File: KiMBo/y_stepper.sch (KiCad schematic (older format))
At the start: 25 parts, among them U24 TMC2130

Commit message: Assocate more footprints
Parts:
- C181, C182: footprint Capacitors_SMD:C_0402 -> Capacitors_SMD:C_0603
- R173, R174, R175, R176, R177, R178: footprint (none) -> Resistors_SMD:R_0603
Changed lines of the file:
@@
 F 0 "C182" H 8315 4346 50  0000 L CNN
 F 1 "22nF" H 8315 4255 50  0000 L CNN
-F 2 "Capacitors_SMD:C_0402" H 8238 4150 50  0001 C CNN
+F 2 "Capacitors_SMD:C_0603" H 8238 4150 50  0001 C CNN
 F 3 "" H 8200 4300 50  0000 C CNN
 	1    8200 4300
@@
 F 0 "R176" V 6250 3900 50  0000 C CNN
 F 1 "2.2Ω" V 6350 3900 50  0000 C CNN
-F 2 "" V 6280 3900 50  0001 C CNN
+F 2 "Resistors_SMD:R_0603" V 6280 3900 50  0001 C CNN
 F 3 "" H 6350 3900 50  0000 C CNN
 	1    6350 3900
@@
 F 0 "R174" H 5169 4446 50  0000 L CNN
 F 1 "4.7kΩ" H 5169 4355 50  0000 L CNN
-F 2 "" V 5030 4400 50  0001 C CNN
+F 2 "Resistors_SMD:R_0603" V 5030 4400 50  0001 C CNN
 F 3 "" H 5100 4400 50  0000 C CNN
 	1    5100 4400
@@
 F 0 "C181" H 6600 4200 50  0000 L CNN
 F 1 "4.7μF" H 6600 4000 50  0000 L CNN
-F 2 "Capacitors_SMD:C_0402" H 6588 3950 50  0001 C CNN
+F 2 "Capacitors_SMD:C_0603" H 6588 3950 50  0001 C CNN
 F 3 "" H 6550 4100 50  0000 C CNN
 	1    6550 4100
@@
 F 0 "R177" H 8369 6896 50  0000 L CNN
 F 1 "5.23kΩ" H 8369 6805 50  0000 L CNN
-F 2 "" V 8230 6850 50  0001 C CNN
+F 2 "Resistors_SMD:R_0603" V 8230 6850 50  0001 C CNN
 F 3 "" H 8300 6850 50  0000 C CNN
 	1    8300 6850
@@
 F 0 "R178" V 8300 7050 50  0000 C CNN
 F 1 "4.75kΩ" V 8400 7050 50  0000 C CNN
-F 2 "" V 8430 7050 50  0001 C CNN
+F 2 "Resistors_SMD:R_0603" V 8430 7050 50  0001 C CNN
 F 3 "" H 8500 7050 50  0000 C CNN
 	1    8500 7050
@@
 F 0 "R175" H 5519 4446 50  0000 L CNN
 F 1 "4.7kΩ" H 5519 4355 50  0000 L CNN
-F 2 "" V 5380 4400 50  0001 C CNN
+F 2 "Resistors_SMD:R_0603" V 5380 4400 50  0001 C CNN
 F 3 "" H 5450 4400 50  0000 C CNN
 	1    5450 4400
@@
 F 0 "R173" H 4819 4446 50  0000 L CNN
 F 1 "4.7kΩ" H 4819 4355 50  0000 L CNN
-F 2 "" V 4680 4400 50  0001 C CNN
+F 2 "Resistors_SMD:R_0603" V 4680 4400 50  0001 C CNN
 F 3 "" H 4750 4400 50  0000 C CNN
 	1    4750 4400

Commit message: More footprint association
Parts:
- R179, R180: footprint (none) -> Resistors_SMD:R_0805
- U24: footprint (none) -> KiMBo:QFN36_5X6
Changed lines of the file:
@@
 $EndComp
 $Comp
-L GND #PWR0242
+L GND #PWR0243
 U 1 1 58C0B231
 P 6550 3450
-F 0 "#PWR0242" H 6550 3200 50  0001 C CNN
+F 0 "#PWR0243" H 6550 3200 50  0001 C CNN
 F 1 "GND" H 6550 3300 50  0000 C CNN
 F 2 "" H 6550 3450 50  0000 C CNN
@@
 $EndComp
 $Comp
-L GND #PWR0243
+L GND #PWR0244
 U 1 1 58C0B23E
 P 9400 3500
-F 0 "#PWR0243" H 9400 3250 50  0001 C CNN
+F 0 "#PWR0244" H 9400 3250 50  0001 C CNN
 F 1 "GND" H 9405 3327 50  0000 C CNN
 F 2 "" H 9400 3500 50  0000 C CNN
@@
 $EndComp
 $Comp
-L +24V #PWR0244
+L +24V #PWR0245
 U 1 1 58C0B244
 P 7600 3000
-F 0 "#PWR0244" H 7600 2850 50  0001 C CNN
+F 0 "#PWR0245" H 7600 2850 50  0001 C CNN
 F 1 "+24V" H 7615 3173 50  0000 C CNN
 F 2 "" H 7600 3000 50  0000 C CNN
@@
 F 0 "R180" H 9750 6800 50  0000 R CNN
 F 1 "220mΩ" H 9750 6900 50  0000 R CNN
-F 2 "" V 9730 6850 50  0001 C CNN
+F 2 "Resistors_SMD:R_0805" V 9730 6850 50  0001 C CNN
 F 3 "" H 9800 6850 50  0000 C CNN
 	1    9800 6850
@@
 F 0 "R179" H 8950 6800 50  0000 R CNN
 F 1 "220mΩ" H 8950 6900 50  0000 R CNN
-F 2 "" V 8930 6850 50  0001 C CNN
+F 2 "Resistors_SMD:R_0805" V 8930 6850 50  0001 C CNN
 F 3 "" H 9000 6850 50  0000 C CNN
 	1    9000 6850
@@
 $EndComp
 $Comp
-L GND #PWR0245
+L GND #PWR0246
 U 1 1 58C0B25F
 P 8700 7200
-F 0 "#PWR0245" H 8700 6950 50  0001 C CNN
+F 0 "#PWR0246" H 8700 6950 50  0001 C CNN
 F 1 "GND" H 8705 7027 50  0000 C CNN
 F 2 "" H 8700 7200 50  0000 C CNN
@@
 NoConn ~ 6750 5850
 $Comp
-L GND #PWR0246
+L GND #PWR0247
 U 1 1 58C0B282
 P 6700 6250
-F 0 "#PWR0246" H 6700 6000 50  0001 C CNN
+F 0 "#PWR0247" H 6700 6000 50  0001 C CNN
 F 1 "GND" H 6705 6077 50  0000 C CNN
 F 2 "" H 6700 6250 50  0000 C CNN
@@
 $EndComp
 $Comp
-L GND #PWR0247
+L GND #PWR0248
 U 1 1 58C0B2C6
 P 8300 5350
-F 0 "#PWR0247" H 8300 5100 50  0001 C CNN
+F 0 "#PWR0248" H 8300 5100 50  0001 C CNN
 F 1 "GND" H 8300 5200 50  0000 C CNN
 F 2 "" H 8300 5350 50  0000 C CNN
@@
 $EndComp
 $Comp
-L GND #PWR0248
+L GND #PWR0249
 U 1 1 58C0B2DA
 P 8300 6200
-F 0 "#PWR0248" H 8300 5950 50  0001 C CNN
+F 0 "#PWR0249" H 8300 5950 50  0001 C CNN
 F 1 "GND" H 8300 6050 50  0000 C CNN
 F 2 "" H 8300 6200 50  0000 C CNN
@@
 F 0 "U24" H 7000 6350 60  0000 C CNN
 F 1 "TMC2130" H 7750 6350 60  0000 C CNN
-F 2 "" H 7450 5150 60  0001 C CNN
+F 2 "KiMBo:QFN36_5X6" H 7450 5150 60  0001 C CNN
 F 3 "" H 7450 5150 60  0000 C CNN
 	1    7450 4850
@@
 	4750 3650 6750 3650
 $Comp
-L VDD_3V3B #PWR0249
+L VDD_3V3B #PWR0250
 U 1 1 5A300CA5
 P 5800 3600
-F 0 "#PWR0249" H 5800 3450 50  0001 C CNN
+F 0 "#PWR0250" H 5800 3450 50  0001 C CNN
 F 1 "VDD_3V3B" H 5815 3773 50  0000 C CNN
 F 2 "" H 5800 3600 50  0000 C CNN

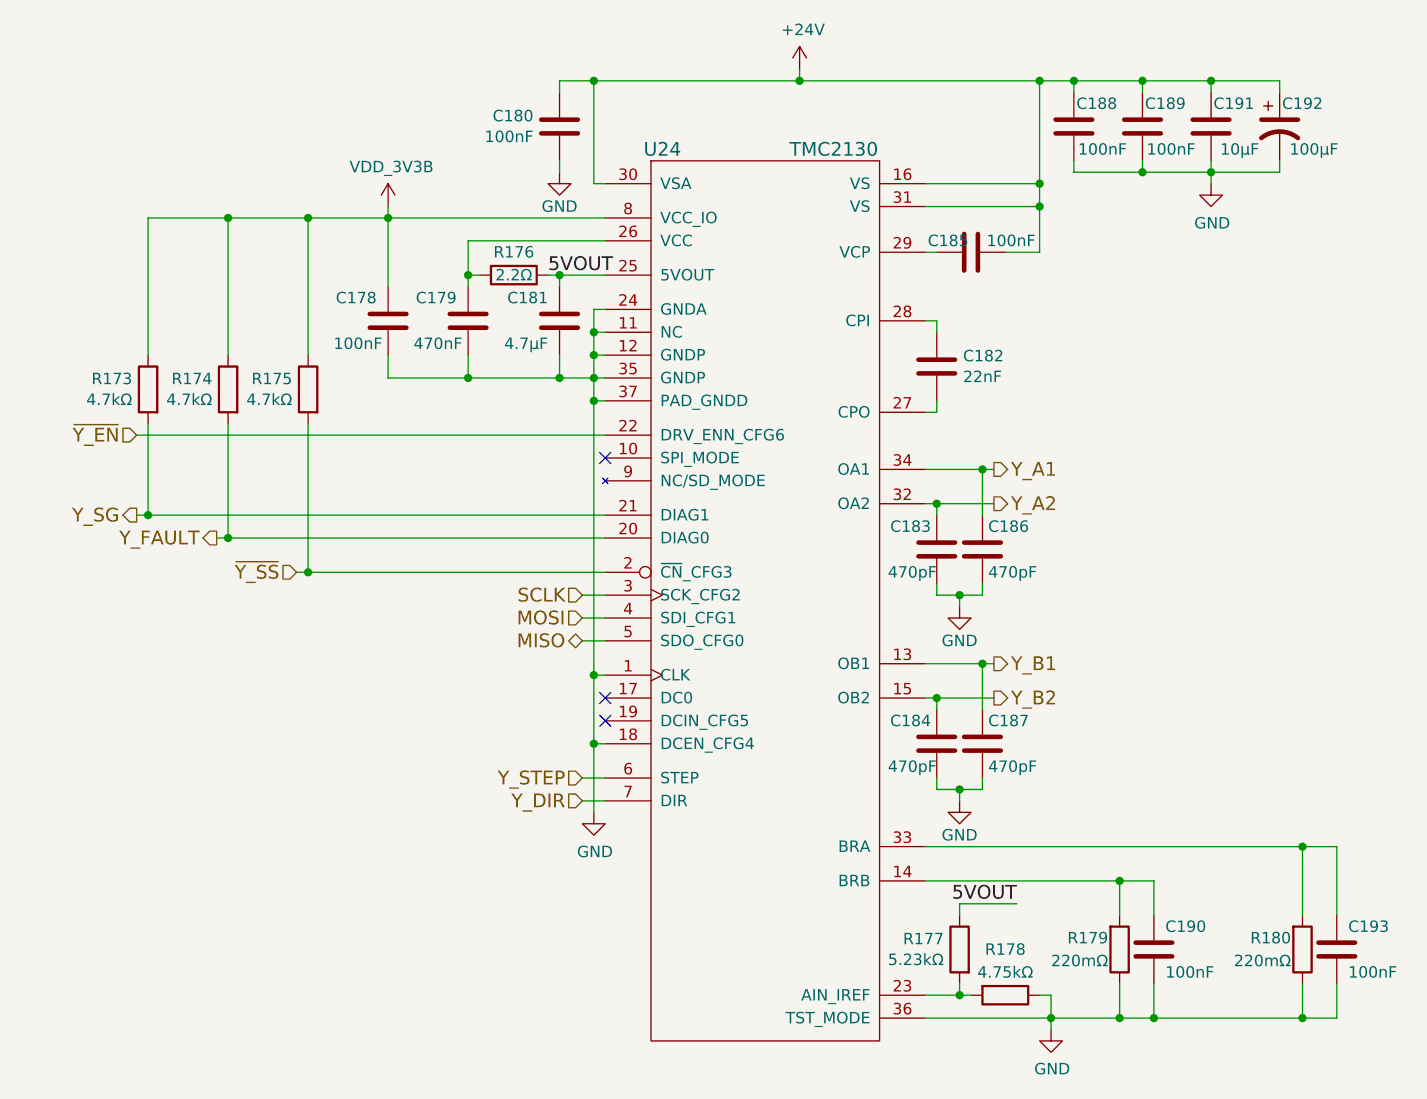
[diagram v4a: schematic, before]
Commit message: Add more footprints and more associations, one association left!
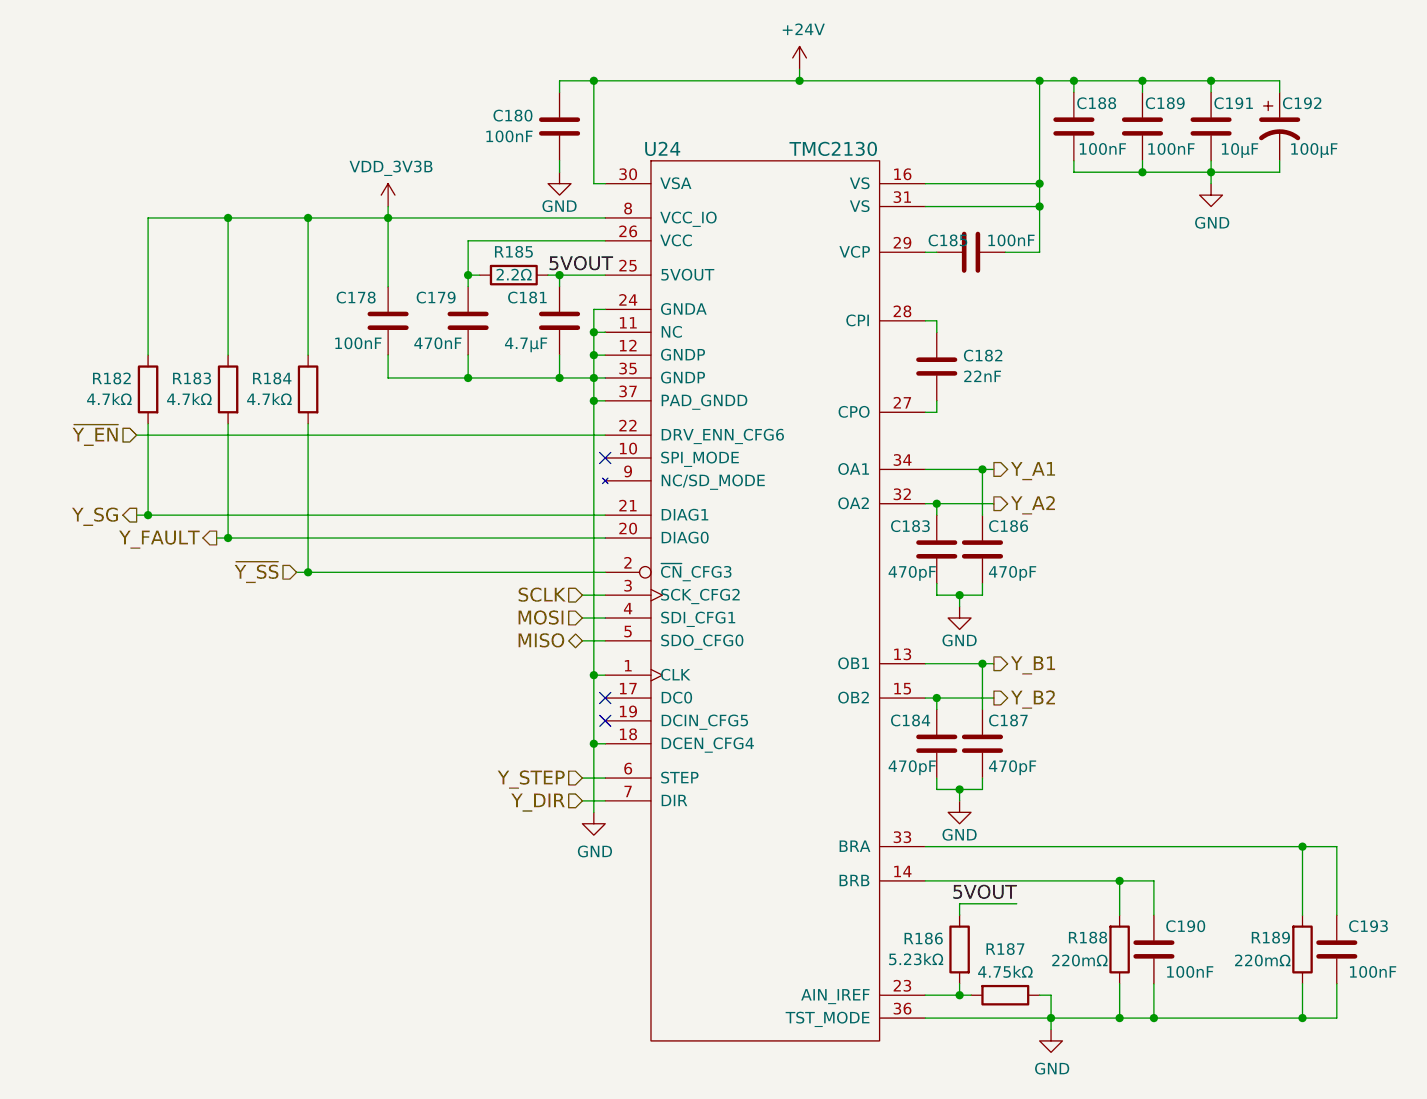
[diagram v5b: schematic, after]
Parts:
- R187: renamed from R178; footprint Resistors_SMD:R_0603 -> Resistors_SMD:R_0805
- R189: renamed from R180; footprint Resistors_SMD:R_0805 -> Resistors_SMD:R_0603
- renumbered R173 to R182, R174 to R183, R175 to R184, R176 to R185, R177 to R186, R179 to R188
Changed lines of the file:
@@
 $EndComp
 $Comp
-L GND #PWR0243
+L GND #PWR0245
 U 1 1 58C0B231
 P 6550 3450
-F 0 "#PWR0243" H 6550 3200 50  0001 C CNN
+F 0 "#PWR0245" H 6550 3200 50  0001 C CNN
 F 1 "GND" H 6550 3300 50  0000 C CNN
 F 2 "" H 6550 3450 50  0000 C CNN
@@
 $EndComp
 $Comp
-L GND #PWR0244
+L GND #PWR0246
 U 1 1 58C0B23E
 P 9400 3500
-F 0 "#PWR0244" H 9400 3250 50  0001 C CNN
+F 0 "#PWR0246" H 9400 3250 50  0001 C CNN
 F 1 "GND" H 9405 3327 50  0000 C CNN
 F 2 "" H 9400 3500 50  0000 C CNN
@@
 $EndComp
 $Comp
-L +24V #PWR0245
+L +24V #PWR0247
 U 1 1 58C0B244
 P 7600 3000
-F 0 "#PWR0245" H 7600 2850 50  0001 C CNN
+F 0 "#PWR0247" H 7600 2850 50  0001 C CNN
 F 1 "+24V" H 7615 3173 50  0000 C CNN
 F 2 "" H 7600 3000 50  0000 C CNN
@@
 $EndComp
 $Comp
-L R R180
+L R R189
 U 1 1 58C0B251
 P 9800 6850
-F 0 "R180" H 9750 6800 50  0000 R CNN
+F 0 "R189" H 9750 6800 50  0000 R CNN
 F 1 "220mΩ" H 9750 6900 50  0000 R CNN
-F 2 "Resistors_SMD:R_0805" V 9730 6850 50  0001 C CNN
+F 2 "Resistors_SMD:R_0603" V 9730 6850 50  0001 C CNN
 F 3 "" H 9800 6850 50  0000 C CNN
 	1    9800 6850
@@
 $EndComp
 $Comp
-L R R179
+L R R188
 U 1 1 58C0B258
 P 9000 6850
-F 0 "R179" H 8950 6800 50  0000 R CNN
+F 0 "R188" H 8950 6800 50  0000 R CNN
 F 1 "220mΩ" H 8950 6900 50  0000 R CNN
 F 2 "Resistors_SMD:R_0805" V 8930 6850 50  0001 C CNN
@@
 $EndComp
 $Comp
-L GND #PWR0246
+L GND #PWR0248
 U 1 1 58C0B25F
 P 8700 7200
-F 0 "#PWR0246" H 8700 6950 50  0001 C CNN
+F 0 "#PWR0248" H 8700 6950 50  0001 C CNN
 F 1 "GND" H 8705 7027 50  0000 C CNN
 F 2 "" H 8700 7200 50  0000 C CNN
@@
 NoConn ~ 6750 5750
 $Comp
-L R R176
+L R R185
 U 1 1 58C0B266
 P 6350 3900
-F 0 "R176" V 6250 3900 50  0000 C CNN
+F 0 "R185" V 6250 3900 50  0000 C CNN
 F 1 "2.2Ω" V 6350 3900 50  0000 C CNN
 F 2 "Resistors_SMD:R_0603" V 6280 3900 50  0001 C CNN
@@
 NoConn ~ 6750 5850
 $Comp
-L GND #PWR0247
+L GND #PWR0249
 U 1 1 58C0B282
 P 6700 6250
-F 0 "#PWR0247" H 6700 6000 50  0001 C CNN
+F 0 "#PWR0249" H 6700 6000 50  0001 C CNN
 F 1 "GND" H 6705 6077 50  0000 C CNN
 F 2 "" H 6700 6250 50  0000 C CNN
@@
 Y_FAULT
 $Comp
-L R R174
+L R R183
 U 1 1 58C0B290
 P 5100 4400
-F 0 "R174" H 5169 4446 50  0000 L CNN
+F 0 "R183" H 5169 4446 50  0000 L CNN
 F 1 "4.7kΩ" H 5169 4355 50  0000 L CNN
 F 2 "Resistors_SMD:R_0603" V 5030 4400 50  0001 C CNN
@@
 5VOUT
 $Comp
-L R R177
+L R R186
 U 1 1 58C0B2A2
 P 8300 6850
-F 0 "R177" H 8369 6896 50  0000 L CNN
+F 0 "R186" H 8369 6896 50  0000 L CNN
 F 1 "5.23kΩ" H 8369 6805 50  0000 L CNN
 F 2 "Resistors_SMD:R_0603" V 8230 6850 50  0001 C CNN
@@
 5VOUT
 $Comp
-L R R178
+L R R187
 U 1 1 58C0B2AA
 P 8500 7050
-F 0 "R178" V 8300 7050 50  0000 C CNN
+F 0 "R187" V 8300 7050 50  0000 C CNN
 F 1 "4.75kΩ" V 8400 7050 50  0000 C CNN
-F 2 "Resistors_SMD:R_0603" V 8430 7050 50  0001 C CNN
+F 2 "Resistors_SMD:R_0805" V 8430 7050 50  0001 C CNN
 F 3 "" H 8500 7050 50  0000 C CNN
 	1    8500 7050
@@
 $EndComp
 $Comp
-L R R175
+L R R184
 U 1 1 58C0B2B1
 P 5450 4400
-F 0 "R175" H 5519 4446 50  0000 L CNN
+F 0 "R184" H 5519 4446 50  0000 L CNN
 F 1 "4.7kΩ" H 5519 4355 50  0000 L CNN
 F 2 "Resistors_SMD:R_0603" V 5380 4400 50  0001 C CNN
@@
 $EndComp
 $Comp
-L GND #PWR0248
+L GND #PWR0250
 U 1 1 58C0B2C6
 P 8300 5350
-F 0 "#PWR0248" H 8300 5100 50  0001 C CNN
+F 0 "#PWR0250" H 8300 5100 50  0001 C CNN
 F 1 "GND" H 8300 5200 50  0000 C CNN
 F 2 "" H 8300 5350 50  0000 C CNN
@@
 $EndComp
 $Comp
-L GND #PWR0249
+L GND #PWR0251
 U 1 1 58C0B2DA
 P 8300 6200
-F 0 "#PWR0249" H 8300 5950 50  0001 C CNN
+F 0 "#PWR0251" H 8300 5950 50  0001 C CNN
 F 1 "GND" H 8300 6050 50  0000 C CNN
 F 2 "" H 8300 6200 50  0000 C CNN
@@
 	8200 6150 8200 6100
 $Comp
-L R R173
+L R R182
 U 1 1 58C0B35B
 P 4750 4400
-F 0 "R173" H 4819 4446 50  0000 L CNN
+F 0 "R182" H 4819 4446 50  0000 L CNN
 F 1 "4.7kΩ" H 4819 4355 50  0000 L CNN
 F 2 "Resistors_SMD:R_0603" V 4680 4400 50  0001 C CNN
@@
 	4750 3650 6750 3650
 $Comp
-L VDD_3V3B #PWR0250
+L VDD_3V3B #PWR0252
 U 1 1 5A300CA5
 P 5800 3600
-F 0 "#PWR0250" H 5800 3450 50  0001 C CNN
+F 0 "#PWR0252" H 5800 3450 50  0001 C CNN
 F 1 "VDD_3V3B" H 5815 3773 50  0000 C CNN
 F 2 "" H 5800 3600 50  0000 C CNN
